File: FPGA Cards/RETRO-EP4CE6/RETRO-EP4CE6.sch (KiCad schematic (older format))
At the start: 32 parts, among them CON1 SD_Card-conn, J1 DCJ0202, J2 Conn_01x04, P1 CONN_02X22, P10 CONN_6, P2 CONN_02X22, P3 Conn_02x13_Odd_Even, P4 Conn_02x12_Odd_Even, P9 VGA, U1 AP1117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

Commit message: pics of cards
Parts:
- R3, R5: value 470 -> 680
- R4, R6: value 680 -> 470
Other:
- moved on the sheet: R3, R4, R5, R6
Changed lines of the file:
@@
 	9700 4150 8850 4150
 Wire Wire Line
+	12650 1950 11800 1950
+Wire Wire Line
 	12650 1750 11800 1750
-Wire Wire Line
-	12650 1950 11800 1950
 Wire Wire Line
 	13500 2750 11800 2750
@@
 Text Label 11900 950  0    60   ~ 0
 P112
-Text Label 11900 1550 0    60   ~ 0
+Text Label 11900 1350 0    60   ~ 0
 P114
 Text Label 11950 2750 0    60   ~ 0
@@
 	12650 950  11800 950
 Wire Wire Line
-	12650 1550 11800 1550
+	12650 1350 11800 1350
 Wire Wire Line
 	3200 7950 2050 7950
@@
 Text Label 11900 1150 0    60   ~ 0
 P113
-Text Label 11900 1350 0    60   ~ 0
+Text Label 11900 1550 0    60   ~ 0
 P115
+Text Label 11900 1950 0    60   ~ 0
+P120
 Text Label 11900 1750 0    60   ~ 0
-P120
-Text Label 11900 1950 0    60   ~ 0
 P124
 Text Label 7650 1900 0    60   ~ 0
@@
 L RETRO-EP4CE6-rescue:R-EP2C5-DB R3
 U 1 1 5D00C5AC
+P 12900 1550
+F 0 "R3" V 12850 1750 40  0000 C CNN
+F 1 "680" V 12900 1550 40  0000 C CNN
+F 2 "Resistor_SMD:R_0805_2012Metric_Pad1.15x1.40mm_HandSolder" V 12799 1550 30  0000 C CNN
+F 3 "" H 12900 1550 30  0000 C CNN
+	1    12900 1550
+	0    1    1    0
+$EndComp
+$Comp
+L RETRO-EP4CE6-rescue:R-EP2C5-DB R4
+U 1 1 5D00C5FE
 P 12900 1350
-F 0 "R3" V 12850 1550 40  0000 C CNN
+F 0 "R4" V 12850 1550 40  0000 C CNN
 F 1 "470" V 12900 1350 40  0000 C CNN
 F 2 "Resistor_SMD:R_0805_2012Metric_Pad1.15x1.40mm_HandSolder" V 12799 1350 30  0000 C CNN
@@
 $EndComp
 $Comp
-L RETRO-EP4CE6-rescue:R-EP2C5-DB R4
-U 1 1 5D00C5FE
-P 12900 1550
-F 0 "R4" V 12850 1750 40  0000 C CNN
-F 1 "680" V 12900 1550 40  0000 C CNN
-F 2 "Resistor_SMD:R_0805_2012Metric_Pad1.15x1.40mm_HandSolder" V 12799 1550 30  0000 C CNN
-F 3 "" H 12900 1550 30  0000 C CNN
-	1    12900 1550
-	0    1    1    0
-$EndComp
-$Comp
 L RETRO-EP4CE6-rescue:R-EP2C5-DB R5
 U 1 1 5D00C652
+P 12900 1950
+F 0 "R5" V 12850 2150 40  0000 C CNN
+F 1 "680" V 12900 1950 40  0000 C CNN
+F 2 "Resistor_SMD:R_0805_2012Metric_Pad1.15x1.40mm_HandSolder" V 12799 1950 30  0000 C CNN
+F 3 "" H 12900 1950 30  0000 C CNN
+	1    12900 1950
+	0    1    1    0
+$EndComp
+$Comp
+L RETRO-EP4CE6-rescue:R-EP2C5-DB R6
+U 1 1 5D00C6A8
 P 12900 1750
-F 0 "R5" V 12850 1950 40  0000 C CNN
+F 0 "R6" V 12850 1950 40  0000 C CNN
 F 1 "470" V 12900 1750 40  0000 C CNN
 F 2 "Resistor_SMD:R_0805_2012Metric_Pad1.15x1.40mm_HandSolder" V 12799 1750 30  0000 C CNN
@@
 	0    1    1    0
 $EndComp
-$Comp
-L RETRO-EP4CE6-rescue:R-EP2C5-DB R6
-U 1 1 5D00C6A8
-P 12900 1950
-F 0 "R6" V 12850 2150 40  0000 C CNN
-F 1 "680" V 12900 1950 40  0000 C CNN
-F 2 "Resistor_SMD:R_0805_2012Metric_Pad1.15x1.40mm_HandSolder" V 12799 1950 30  0000 C CNN
-F 3 "" H 12900 1950 30  0000 C CNN
-	1    12900 1950
-	0    1    1    0
-$EndComp
-Wire Wire Line
-	12650 1350 11800 1350
+Wire Wire Line
+	12650 1550 11800 1550
 Wire Wire Line
 	12650 1150 11800 1150
@@
 Text Notes 12200 1750 0    50   ~ 0
 (vgaBluHi)
-Text Notes 12200 1900 0    50   ~ 0
+Text Notes 12200 1950 0    50   ~ 0
 (vgaBluLo)
 Text Notes 12250 2750 0    50   ~ 0

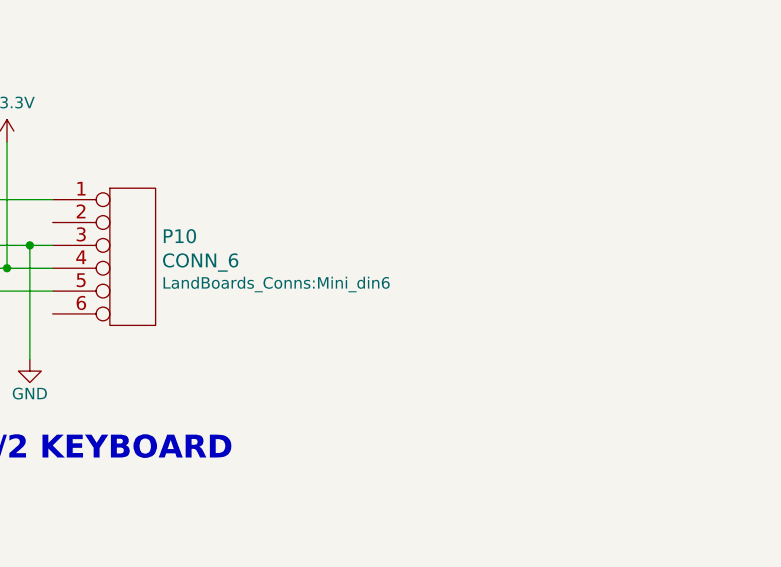
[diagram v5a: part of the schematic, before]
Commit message: fixed ps/2 footprint
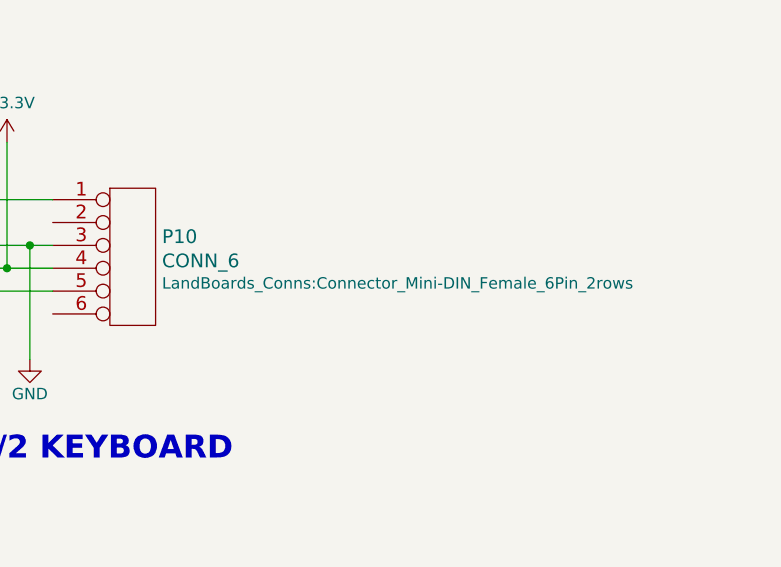
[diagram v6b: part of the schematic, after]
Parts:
- P10: footprint LandBoards_Conns:Mini_din6 -> LandBoards_Conns:Connector_Mini-DIN_Female_6Pin_2rows
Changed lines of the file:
@@
 F 0 "P10" H 14128 8138 60  0000 L CNN
 F 1 "CONN_6" H 14128 8032 60  0000 L CNN
-F 2 "LandBoards_Conns:Mini_din6" H 14128 7934 50  0000 L CNN
+F 2 "LandBoards_Conns:Connector_Mini-DIN_Female_6Pin_2rows" H 14128 7934 50  0000 L CNN
 F 3 "" H 14000 8050 50  0001 C CNN
 	1    14000 8050

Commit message: retro
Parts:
- U2: symbol LandBoards_Semis:IS61WV5128EDBLL-10TLI -> RETRO-EP4CE6-rescue:IS61WV5128EDBLL-10TLI-LandBoards_Semis
- U3: symbol LandBoards_Cards:FTDI_Module -> RETRO-EP4CE6-rescue:FTDI_Module-LandBoards_Cards
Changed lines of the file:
@@
 	8950 1800 8950 2800
 $Comp
-L LandBoards_Semis:IS61WV5128EDBLL-10TLI U2
+L RETRO-EP4CE6-rescue:IS61WV5128EDBLL-10TLI-LandBoards_Semis U2
 U 1 1 5CAA55C2
 P 8550 6800
@@
 Connection ~ 8250 3550
 $Comp
-L LandBoards_Cards:FTDI_Module U3
+L RETRO-EP4CE6-rescue:FTDI_Module-LandBoards_Cards U3
 U 1 1 5CDDC99F
 P 12850 5250

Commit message: Annotated SD Card connections
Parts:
- H1: symbol Connector_Generic:Conn_01x02 -> RETRO-EP4CE6-rescue:Conn_01x02-Connector_Generic
- J2: symbol Connector_Generic:Conn_01x04 -> RETRO-EP4CE6-rescue:Conn_01x04-Connector_Generic
- P3: symbol Connector_Generic:Conn_02x13_Odd_Even -> RETRO-EP4CE6-rescue:Conn_02x13_Odd_Even-Connector_Generic
- P4: symbol Connector_Generic:Conn_02x12_Odd_Even -> RETRO-EP4CE6-rescue:Conn_02x12_Odd_Even-Connector_Generic
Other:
- note added: "MISO"
- note added: "MOSI"
- note added: "SCLK"
- note added: "SDCS"
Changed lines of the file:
@@
 	13650 5750 14750 5750
 $Comp
-L Connector_Generic:Conn_01x02 H1
+L RETRO-EP4CE6-rescue:Conn_01x02-Connector_Generic H1
 U 1 1 5CF16ADC
 P 13300 4550
@@
 	13200 7700 13200 8200
 $Comp
-L Connector_Generic:Conn_01x04 J2
+L RETRO-EP4CE6-rescue:Conn_01x04-Connector_Generic J2
 U 1 1 5CA89AE4
 P 12150 7250
@@
 	13200 8200 13650 8200
 $Comp
-L Connector_Generic:Conn_02x12_Odd_Even P4
+L RETRO-EP4CE6-rescue:Conn_02x12_Odd_Even-Connector_Generic P4
 U 1 1 5CDFF210
 P 8550 3950
@@
 $EndComp
 $Comp
-L Connector_Generic:Conn_02x13_Odd_Even P3
+L RETRO-EP4CE6-rescue:Conn_02x13_Odd_Even-Connector_Generic P3
 U 1 1 5CFCD9D8
 P 8550 2200
@@
 Wire Wire Line
 	8100 2600 8100 1350
+Text Notes 2500 7550 0    50   ~ 0
+SDCS
+Text Notes 2500 7650 0    50   ~ 0
+MOSI
+Text Notes 2500 7950 0    50   ~ 0
+SCLK
+Text Notes 2500 8150 0    50   ~ 0
+MISO
 $EndSCHEMATC
